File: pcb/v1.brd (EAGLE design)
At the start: 92 x 80 mm, 61 parts, among them T1 MMBT3904, T2 MMBT3904, T3 MMBT3904, T4 MMBT3904

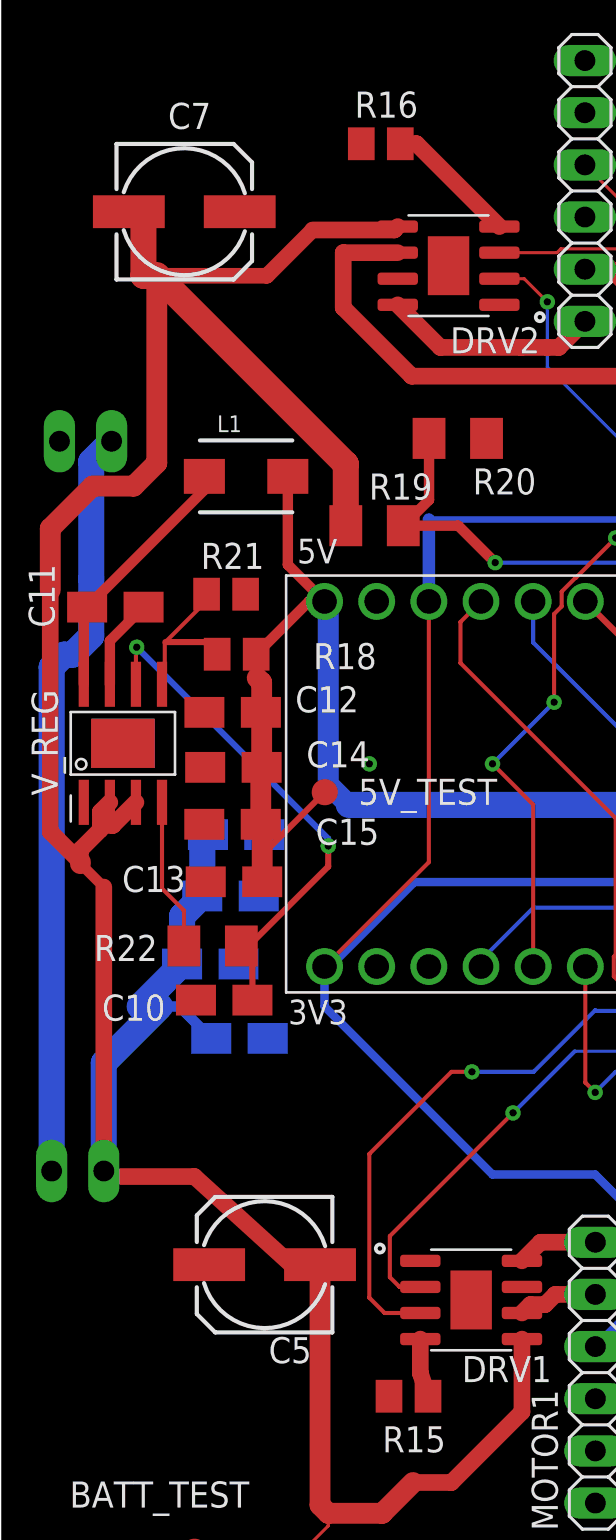
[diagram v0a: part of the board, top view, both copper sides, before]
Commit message: Changed the resistive voltage divider values
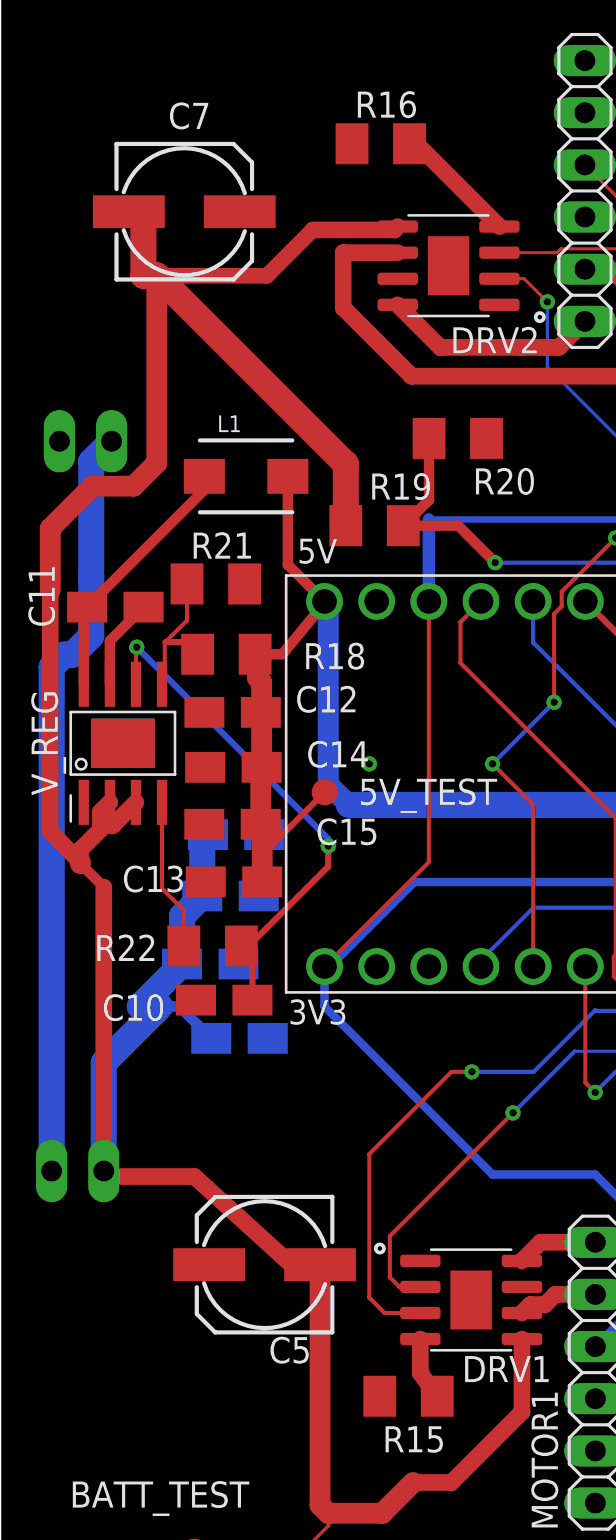
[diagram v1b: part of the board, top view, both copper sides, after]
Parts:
- R15, R16, R18, R21: device rcl:M2012 -> rcl:M1206
- R19: value 500k -> 100k
- R20: value 150k -> 30k
- moved R21 0.71 mm to (10.5, 49.8)
- moved R18 0.50 mm to (11.0, 46.3)
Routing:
- net N$23: track 8.05 -> 7.43 mm
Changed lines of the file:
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@@
 <drawing>
 <settings>
-<setting alwaysvectorfont="yes"/>
+<setting alwaysvectorfont="no"/>
 <setting verticaltext="up"/>
 </settings>
@@
 <attribute name="VALUE" x="69.36198125" y="59.505925" size="1.27" layer="28" rot="MR45"/>
 </element>
-<element name="R15" library="rcl" library_urn="urn:adsk.eagle:library:334" package="M2012" package3d_urn="urn:adsk.eagle:package:23561/1" value="30k" x="19.91" y="10.2" smashed="yes">
+<element name="R15" library="rcl" library_urn="urn:adsk.eagle:library:334" package="M1206" package3d_urn="urn:adsk.eagle:package:23566/1" value="30k" x="19.91" y="10.2" smashed="yes">
 <attribute name="NAME" x="18.64" y="7.47" size="1.27" layer="25"/>
 <attribute name="SPICEPREFIX" value="R" x="80.87" y="-53.3" size="1.778" layer="27" display="off"/>
 <attribute name="VALUE" x="18.64" y="7.66" size="1.27" layer="27"/>
 </element>
-<element name="R16" library="rcl" library_urn="urn:adsk.eagle:library:334" package="M2012" package3d_urn="urn:adsk.eagle:package:23561/1" value="30k" x="18.56" y="71.2" smashed="yes">
+<element name="R16" library="rcl" library_urn="urn:adsk.eagle:library:334" package="M1206" package3d_urn="urn:adsk.eagle:package:23566/1" value="30k" x="18.56" y="71.2" smashed="yes">
 <attribute name="NAME" x="17.29" y="72.47" size="1.27" layer="25"/>
 <attribute name="SPICEPREFIX" value="R" x="85.87" y="7.7" size="1.778" layer="27" display="off"/>
 <attribute name="VALUE" x="17.29" y="68.66" size="1.27" layer="27"/>
 </element>
-<element name="R19" library="rcl" library_urn="urn:adsk.eagle:library:334" package="M1206" package3d_urn="urn:adsk.eagle:package:23566/1" value="500k" x="18.255559375" y="52.59816875" smashed="yes">
+<element name="R19" library="rcl" library_urn="urn:adsk.eagle:library:334" package="M1206" package3d_urn="urn:adsk.eagle:package:23566/1" value="100k" x="18.255559375" y="52.59816875" smashed="yes">
 <attribute name="NAME" x="17.985559375" y="53.86816875" size="1.27" layer="25"/>
 <attribute name="SPICEPREFIX" value="R" x="47.465559375" y="-4.55183125" size="1.778" layer="27" display="off"/>
@@
 <attribute name="VALUE" x="70.15" y="50.12" size="1.27" layer="28" rot="MR270"/>
 </element>
-<element name="R20" library="rcl" library_urn="urn:adsk.eagle:library:334" package="M1206" package3d_urn="urn:adsk.eagle:package:23566/1" value="150k" x="22.31" y="56.85" smashed="yes">
+<element name="R20" library="rcl" library_urn="urn:adsk.eagle:library:334" package="M1206" package3d_urn="urn:adsk.eagle:package:23566/1" value="30k" x="22.31" y="56.85" smashed="yes">
 <attribute name="NAME" x="23.04" y="54.12" size="1.27" layer="25"/>
 <attribute name="SPICEPREFIX" value="R" x="57.87" y="-0.3" size="1.778" layer="27" display="off"/>
@@
 <attribute name="VALUE" x="8.98329375" y="27.166865625" size="1.27" layer="27"/>
 </element>
-<element name="R18" library="rcl" library_urn="urn:adsk.eagle:library:334" package="M2012" package3d_urn="urn:adsk.eagle:package:23561/1" value="100k" x="11.54065625" y="46.338321875" smashed="yes">
-<attribute name="NAME" x="15.27065625" y="45.608321875" size="1.27" layer="25"/>
-<attribute name="SPICEPREFIX" value="R" x="11.54065625" y="46.338321875" size="1.778" layer="27" display="off"/>
-<attribute name="VALUE" x="10.27065625" y="43.798321875" size="1.27" layer="27"/>
-</element>
-<element name="R21" library="rcl" library_urn="urn:adsk.eagle:library:334" package="M2012" package3d_urn="urn:adsk.eagle:package:23561/1" value="24.9k" x="11.0254875" y="49.261846875" smashed="yes" rot="R180">
-<attribute name="NAME" x="9.7954875" y="50.491846875" size="1.27" layer="25"/>
-<attribute name="SPICEPREFIX" value="R" x="11.0254875" y="49.261846875" size="1.778" layer="27" rot="R180" display="off"/>
-<attribute name="VALUE" x="12.2954875" y="51.801846875" size="1.27" layer="27" rot="R180"/>
+<element name="R18" library="rcl" library_urn="urn:adsk.eagle:library:334" package="M1206" package3d_urn="urn:adsk.eagle:package:23566/1" value="100k" x="11.04065625" y="46.338321875" smashed="yes">
+<attribute name="NAME" x="14.77065625" y="45.608321875" size="1.27" layer="25"/>
+<attribute name="SPICEPREFIX" value="R" x="11.04065625" y="46.338321875" size="1.778" layer="27" display="off"/>
+<attribute name="VALUE" x="9.77065625" y="43.798321875" size="1.27" layer="27"/>
+</element>
+<element name="R21" library="rcl" library_urn="urn:adsk.eagle:library:334" package="M1206" package3d_urn="urn:adsk.eagle:package:23566/1" value="24.9k" x="10.5254875" y="49.761846875" smashed="yes" rot="R180">
+<attribute name="NAME" x="9.2954875" y="50.991846875" size="1.27" layer="25"/>
+<attribute name="SPICEPREFIX" value="R" x="10.5254875" y="49.761846875" size="1.778" layer="27" rot="R180" display="off"/>
+<attribute name="VALUE" x="11.7954875" y="52.301846875" size="1.27" layer="27" rot="R180"/>
 </element>
 <element name="C11" library="rcl" library_urn="urn:adsk.eagle:library:334" package="A/3216-18R" package3d_urn="urn:adsk.eagle:package:23410/2" value=".1uF" x="5.632203125" y="48.6322375" smashed="yes">
@@
 <wire x1="14.032" y1="55" x2="14.032" y2="50.69693125" width="0.508" layer="1"/>
 <wire x1="14.032" y1="50.69693125" x2="15.8199875" y2="48.90894375" width="0.508" layer="1"/>
-<wire x1="12.49065625" y1="46.338321875" x2="12.54065625" y2="46.288321875" width="0.508" layer="1"/>
-<wire x1="12.54065625" y1="46.288321875" x2="12.54065625" y2="45.1853625" width="0.508" layer="1"/>
+<wire x1="12.44065625" y1="46.338321875" x2="12.54065625" y2="46.325821875" width="0.508" layer="1"/>
+<wire x1="12.54065625" y1="46.325821875" x2="12.54065625" y2="45.1853625" width="0.508" layer="1"/>
 <wire x1="12.54065625" y1="45.1853625" x2="12.54065625" y2="43.6853625" width="0.508" layer="1"/>
-<wire x1="12.49065625" y1="46.338321875" x2="15.061278125" y2="48.90894375" width="0.508" layer="1"/>
-<wire x1="15.061278125" y1="48.90894375" x2="15.8199875" y2="48.90894375" width="0.508" layer="1"/>
+<wire x1="15.8199875" y1="48.828653125" x2="13.7656" y2="46.338321875" width="0.508" layer="1"/>
+<wire x1="12.44065625" y1="46.338321875" x2="13.7656" y2="46.338321875" width="0.508" layer="1"/>
+<wire x1="15.8199875" y1="48.90894375" x2="15.8199875" y2="48.828653125" width="0.508" layer="1"/>
 </signal>
 <signal name="REC1">
@@
 <contactref element="DRV1" pad="4"/>
 <contactref element="R15" pad="2"/>
-<wire x1="20.86" y1="10.2" x2="20.485" y2="11.325" width="0.8128" layer="1"/>
+<wire x1="21.31" y1="10.2" x2="20.485" y2="11.325" width="0.8128" layer="1"/>
 <wire x1="20.485" y1="11.325" x2="20.485" y2="12.985" width="0.8128" layer="1"/>
 </signal>
@@
 <contactref element="R16" pad="2"/>
 <wire x1="24.335" y1="67.165" x2="20.3" y2="71.2" width="0.8128" layer="1"/>
-<wire x1="20.3" y1="71.2" x2="19.51" y2="71.2" width="0.8128" layer="1"/>
+<wire x1="20.3" y1="71.2" x2="19.96" y2="71.2" width="0.8128" layer="1"/>
 </signal>
 <signal name="T1">
@@
 <contactref element="R21" pad="2"/>
 <wire x1="7.905" y1="44.875" x2="8.039565625" y2="45.009565625" width="0.2" layer="1"/>
-<wire x1="10.0754875" y1="49.261846875" x2="10.0754875" y2="48.9371375" width="0.2" layer="1"/>
-<wire x1="10.0754875" y1="48.9371375" x2="8.069175" y2="46.930825" width="0.2" layer="1"/>
+<wire x1="9.1254875" y1="49.761846875" x2="9.1254875" y2="47.9871375" width="0.2" layer="1"/>
+<wire x1="9.1254875" y1="47.9871375" x2="8.069175" y2="46.930825" width="0.2" layer="1"/>
 <wire x1="8.069175" y1="46.930825" x2="8.039565625" y2="46.901215625" width="0.2" layer="1"/>
 <wire x1="8.039565625" y1="45.009565625" x2="8.039565625" y2="46.901215625" width="0.2" layer="1"/>
-<wire x1="8.069175" y1="46.930825" x2="9.998153125" y2="46.930825" width="0.3" layer="1"/>
-<wire x1="9.998153125" y1="46.930825" x2="10.59065625" y2="46.338321875" width="0.3" layer="1"/>
+<wire x1="8.069175" y1="46.930825" x2="9.498153125" y2="46.930825" width="0.3" layer="1"/>
+<wire x1="9.498153125" y1="46.930825" x2="9.64065625" y2="46.338321875" width="0.3" layer="1"/>
 </signal>
 <signal name="N$25">

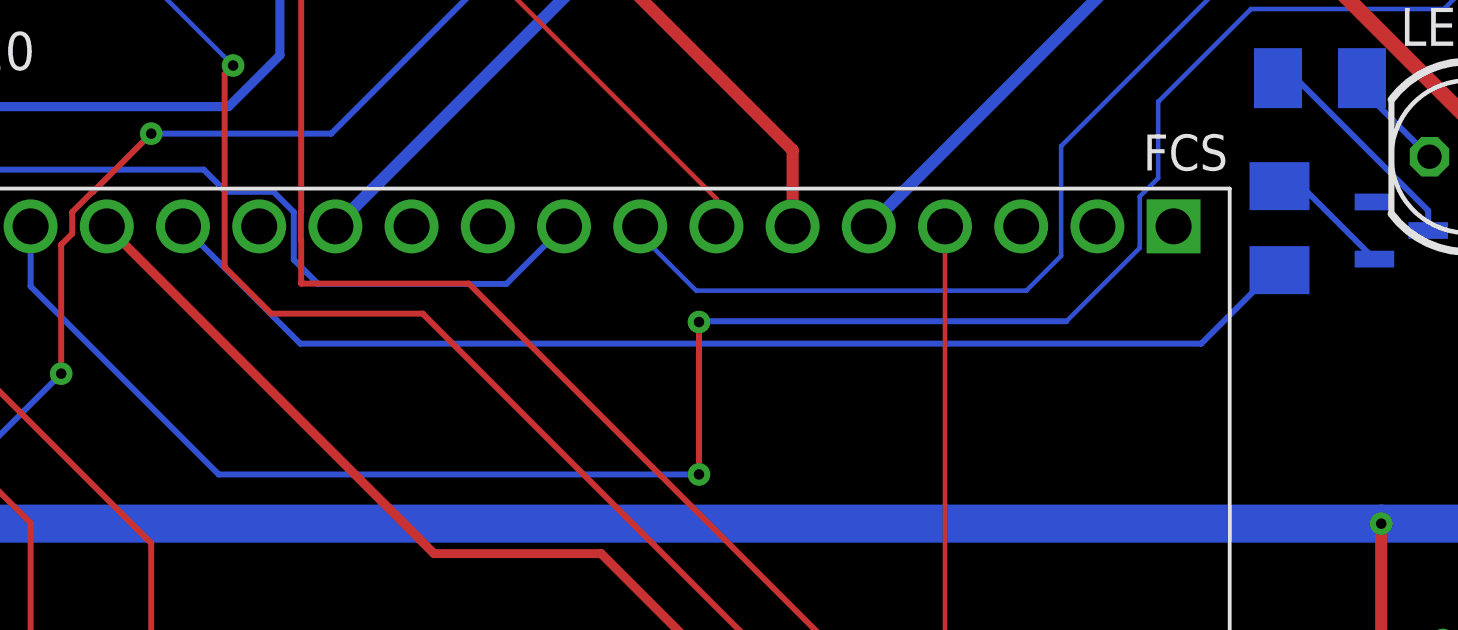
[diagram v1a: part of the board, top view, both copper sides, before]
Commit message: Added ground plane
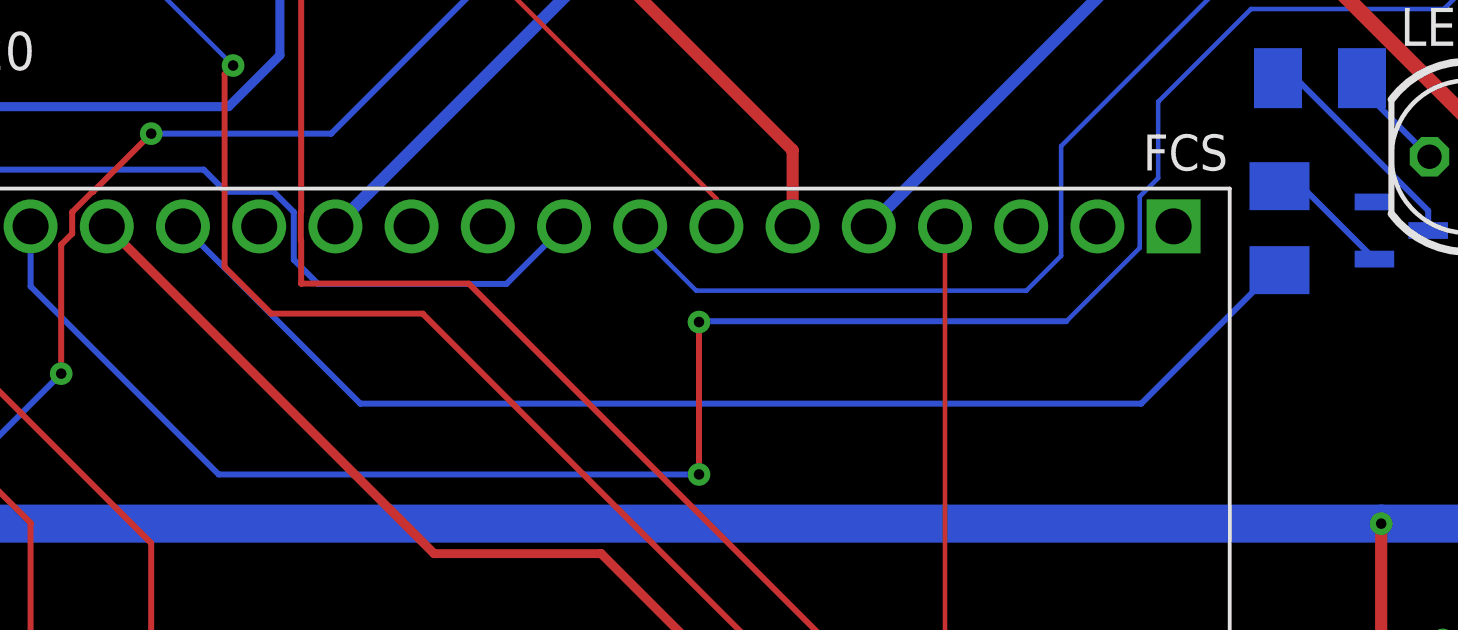
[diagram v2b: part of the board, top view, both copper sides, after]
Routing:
- net EM1: track 39.2 -> 40.8 mm
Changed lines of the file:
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@@
 <contactref element="ESP32" pad="J3_14"/>
 <contactref element="R2" pad="2"/>
-<wire x1="31.0599875" y1="48.90894375" x2="34.96893125" y2="45" width="0.2" layer="16"/>
-<wire x1="65" y1="45" x2="67.45" y2="47.45" width="0.2" layer="16"/>
+<wire x1="31.0599875" y1="48.90894375" x2="36.96893125" y2="43" width="0.2" layer="16"/>
+<wire x1="63" y1="43" x2="67.45" y2="47.45" width="0.2" layer="16"/>
 <wire x1="67.45" y1="47.45" x2="67.61" y2="47.45" width="0.2" layer="16"/>
-<wire x1="34.96893125" y1="45" x2="65" y2="45" width="0.2" layer="16"/>
+<wire x1="36.96893125" y1="43" x2="63" y2="43" width="0.2" layer="16"/>
 </signal>
 <signal name="REC3">

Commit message: Added Strawberry
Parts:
- moved BATT_TEST 2.00 mm to (11.5, 2.63)
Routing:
- net BATT_POWER: track 157.7 -> 155.3 mm
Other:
- board text added: "/Users/vamsighorakavi/Downloads/strawberry(2).bmp"

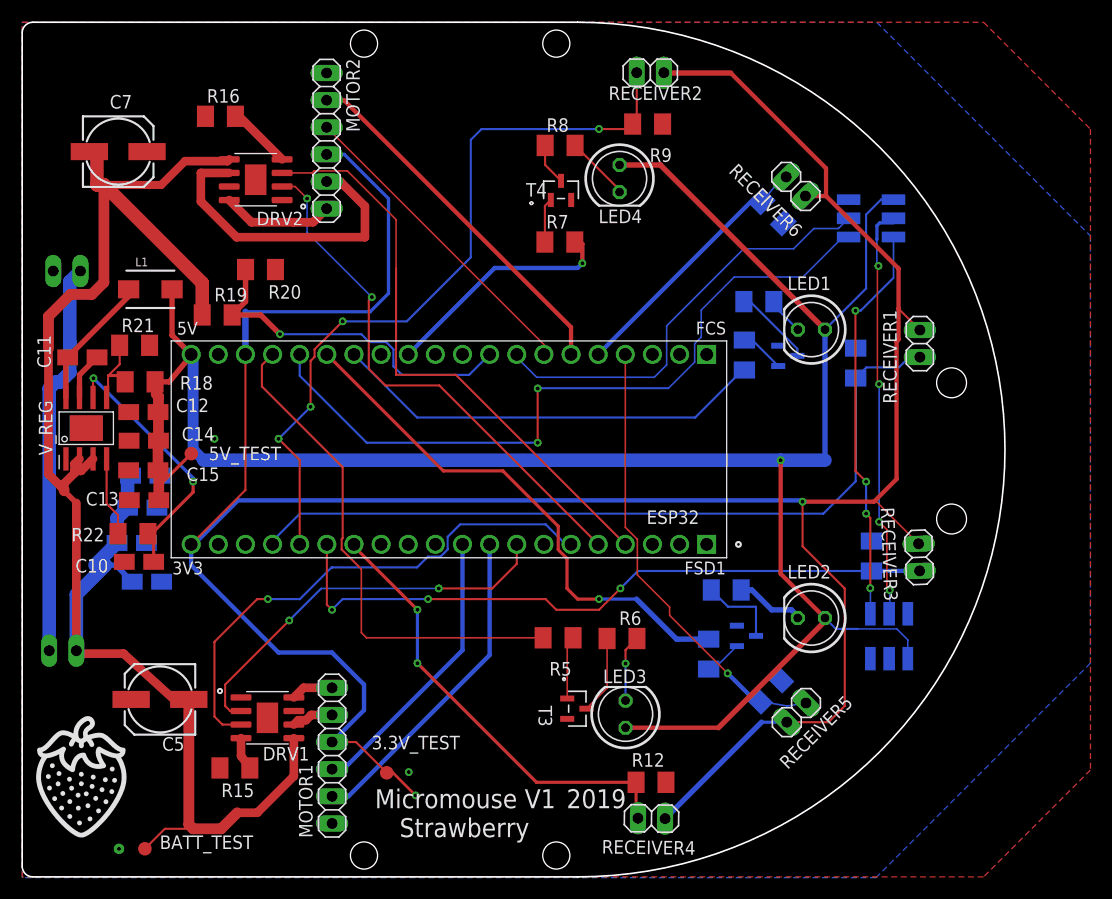
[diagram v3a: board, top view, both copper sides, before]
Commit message: Changed strawberry and caps. Added gerber files
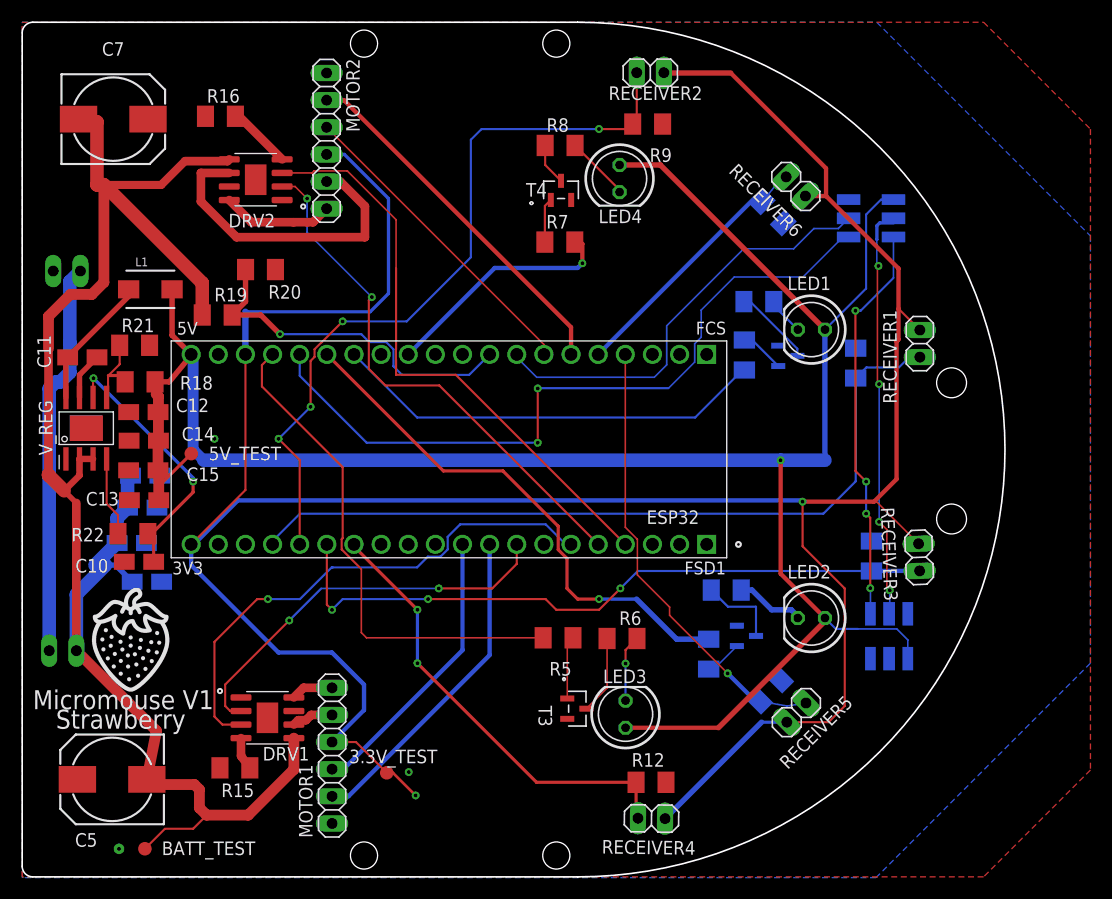
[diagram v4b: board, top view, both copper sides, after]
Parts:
- C5, C7: device rcl:153CLV-0605 -> rcl:150CLZ-0810
- moved C5 8.72 mm to (8.42, 9.12)
- moved C7 3.08 mm to (8.53, 70.9)
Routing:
- net BATT_POWER: track 155.3 -> 156.7 mm
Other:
- board text removed: "2019"
